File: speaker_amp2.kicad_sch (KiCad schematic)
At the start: 30 parts, among them U1 TAS5822MDCPR

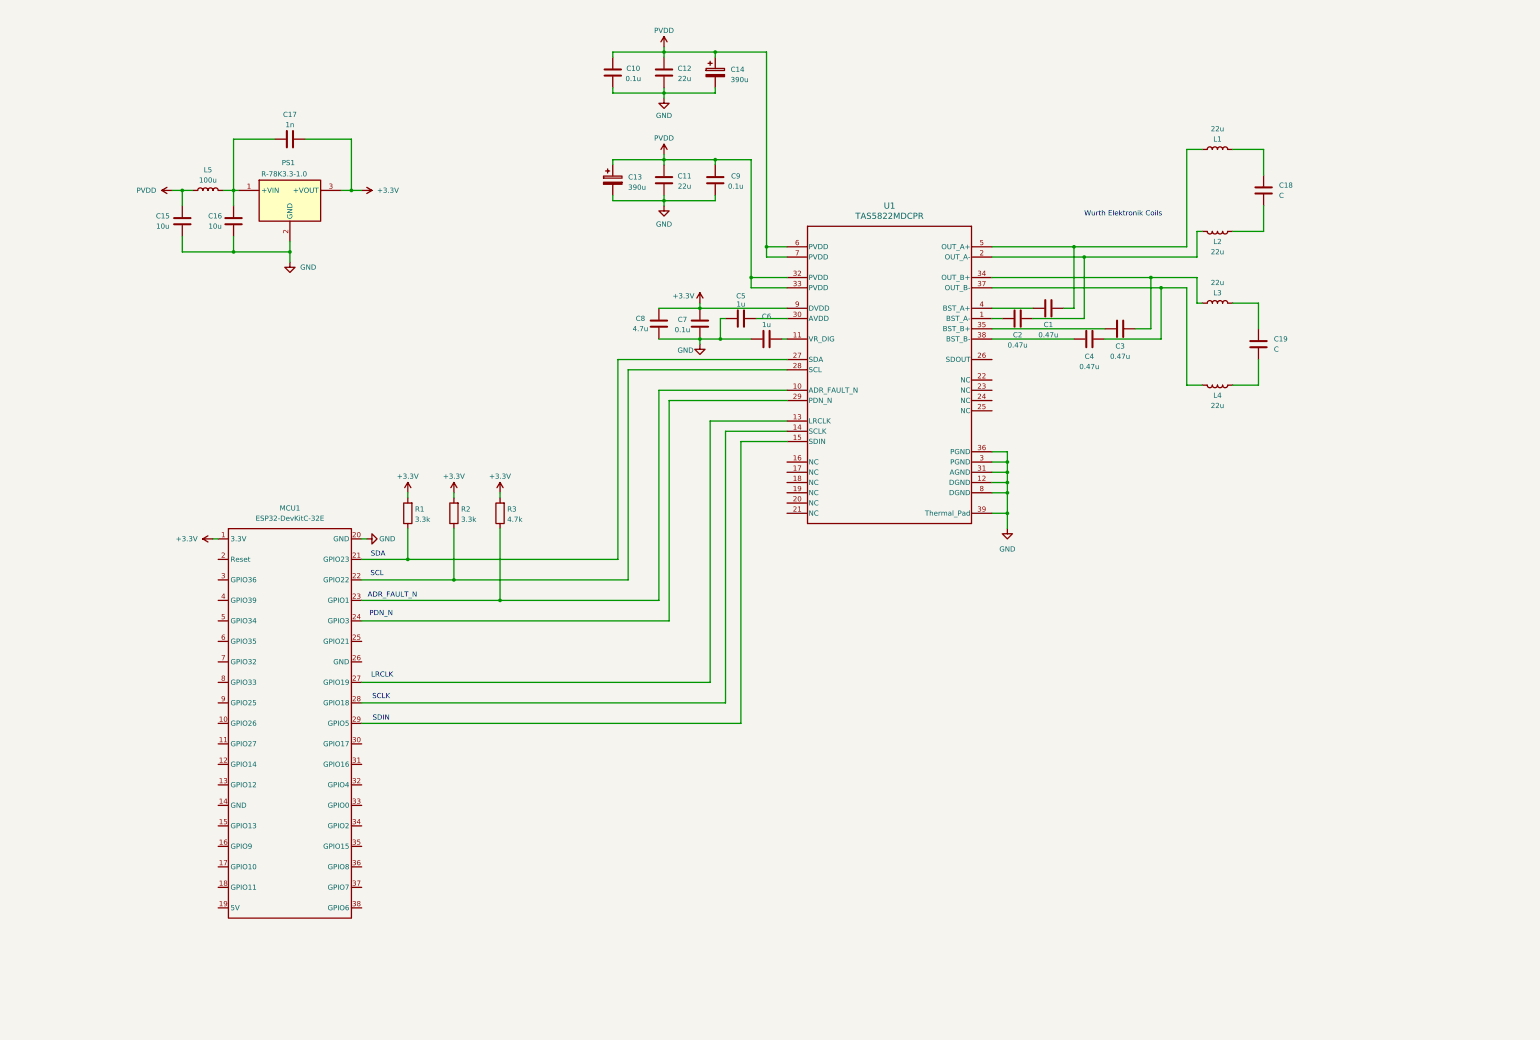
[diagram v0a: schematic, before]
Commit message: added C_g cap
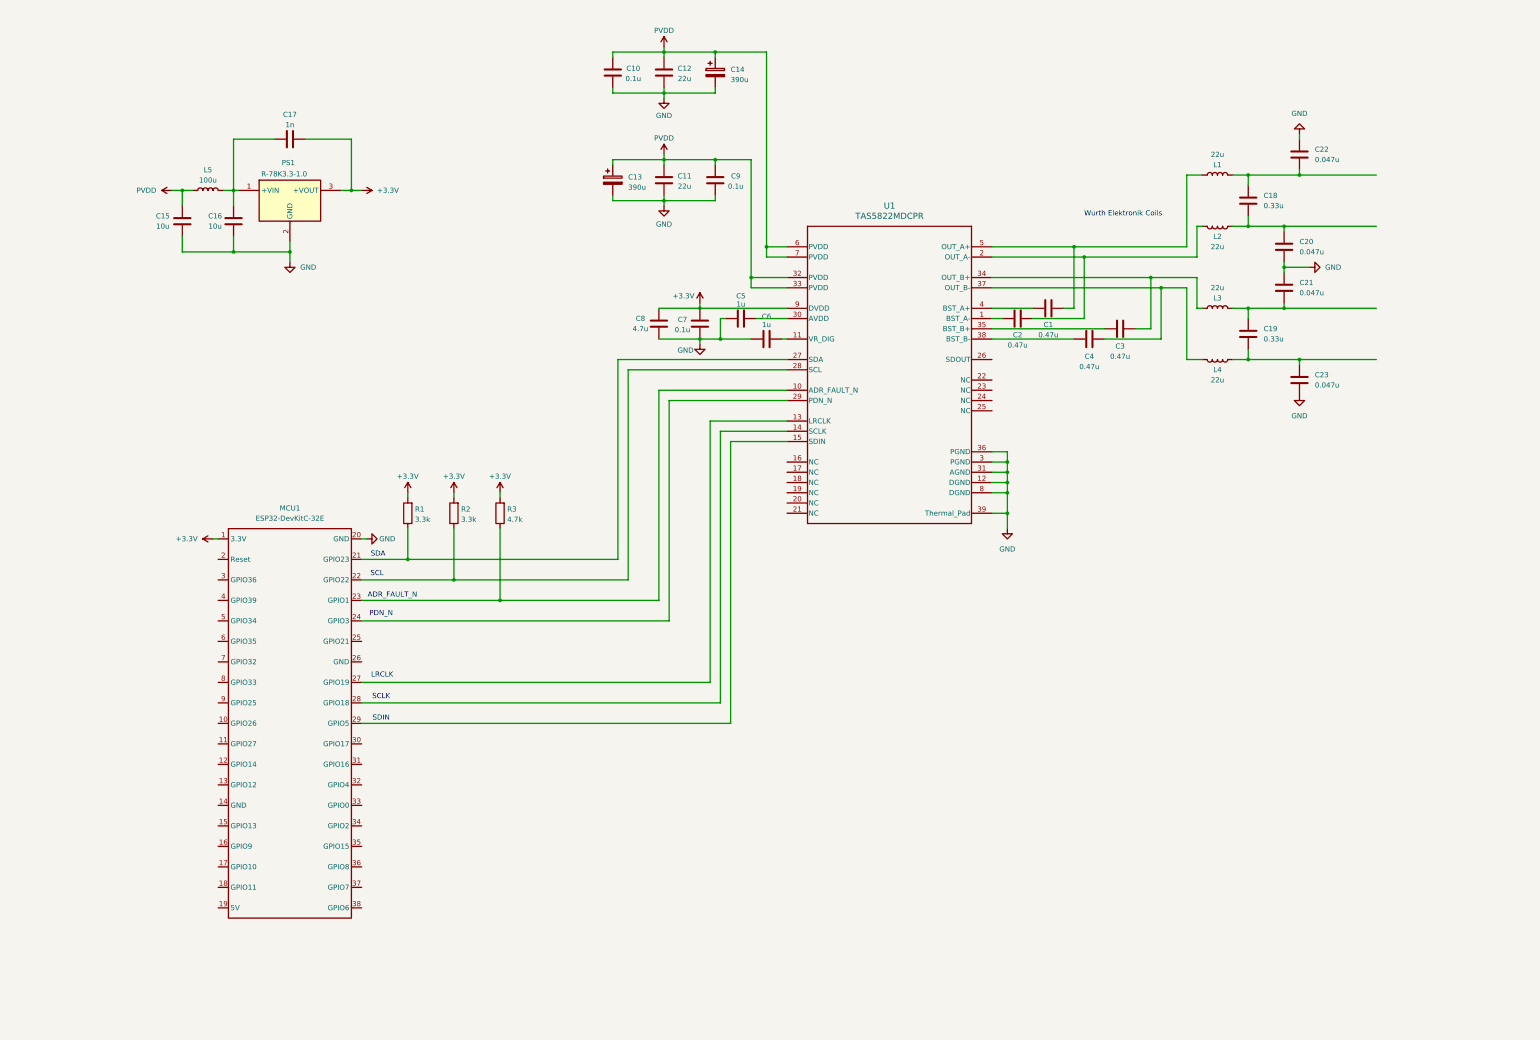
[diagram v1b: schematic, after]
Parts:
- added C20, C21, C22, C23: 0.047u, Capacitor_THT:C_Rect_L13.0mm_W5.0mm_P10.00mm_FKS3_FKP3_MKS4, symbol Device:C
- C18, C19: value C -> 0.33u
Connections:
- net GND: now also C20.2, C21.1, C22.1, C23.2
- net at C18.2, L2.1: now also C20.1
- net at C18.1, L1.2: now also C22.2
- net at C19.2, L4.1: now also C23.1
- net at C19.1, L3.2: now also C21.2
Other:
- moved on the sheet: C18, L1, L2, L3, L4

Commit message: added 2nd TAS5822M
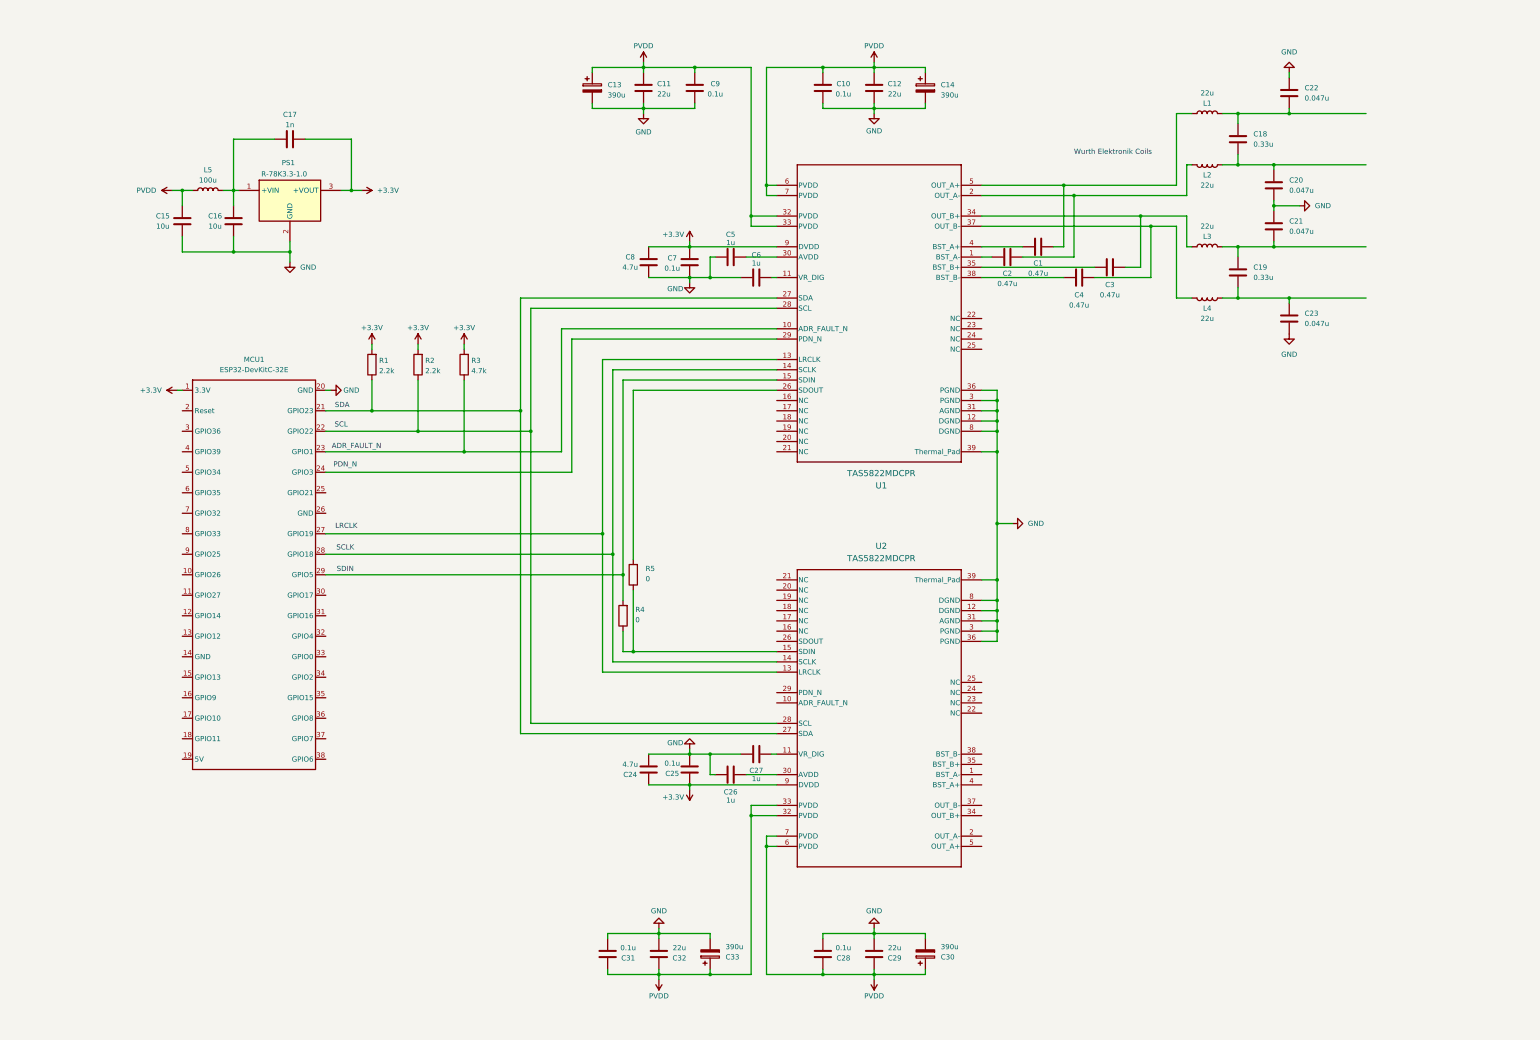
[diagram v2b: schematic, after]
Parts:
- added C24: 4.7u, Capacitor_SMD:C_0805_2012Metric_Pad1.18x1.45mm_HandSolder, symbol Device:C
- added C25, C28, C31: 0.1u, Capacitor_SMD:C_0805_2012Metric_Pad1.18x1.45mm_HandSolder, symbol Device:C
- added C26, C27: 1u, Capacitor_SMD:C_0805_2012Metric_Pad1.18x1.45mm_HandSolder, symbol Device:C
- added C29, C32: 22u, Capacitor_SMD:C_1210_3225Metric_Pad1.33x2.70mm_HandSolder, symbol Device:C
- added C30, C33: 390u, Capacitor_THT:CP_Radial_D8.0mm_P3.50mm, symbol Device:C_Polarized
- added R4, R5: 0, Resistor_SMD:R_0805_2012Metric_Pad1.20x1.40mm_HandSolder, symbol Device:R
- added U2: TAS5822MDCPR, DCP0038A-IPC_A, symbol Speaker Amp Lib:TAS5822MDCPR
- R1, R2: value 3.3k -> 2.2k; MouserLink https://gr.mouser.com/ProductDetail/YAGEO/RT0805DRD073K3L?q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 -> https://gr.mouser.com/ProductDetail/YAGEO/RT0805FRE132K2L?q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
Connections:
- net +3.3V: now also C24.2, C25.2, U2.9 (DVDD)
- net GND: now also C24.1, C25.1, C26.2, C27.2, C28.1, C29.1, C30.2, C31.1, C32.1, C33.2, U2.12 (DGND), U2.3 (PGND), U2.31 (AGND), U2.36 (PGND), U2.39 (Thermal_Pad), U2.8 (DGND)
- net PVDD: now also C28.2, C29.2, C30.1, C31.2, C32.2, C33.1, U2.32 (PVDD), U2.33 (PVDD), U2.6 (PVDD), U2.7 (PVDD)
- net at MCU1.22 (GPIO22), R2.1, U1.28 (SCL): now also U2.28 (SCL)
- net at MCU1.21 (GPIO23), R1.1, U1.27 (SDA): now also U2.27 (SDA)
- net at MCU1.27 (GPIO19), U1.13 (LRCLK): now also U2.13 (LRCLK)
- net at MCU1.28 (GPIO18), U1.14 (SCLK): now also U2.14 (SCLK)
- net at MCU1.29 (GPIO5), U1.15 (SDIN): now also R4.2
- net at U1.26 (SDOUT): now also R5.2
- new net: C26.1, U2.30 (AVDD)
- new net: C27.1, U2.11 (VR_DIG)
- new net: R4.1, R5.1, U2.15 (SDIN)
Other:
- moved on the sheet: C1, C10, C11, C12, C13, C14, C18, C19, C2, C20, C21, C22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

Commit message: added mono ch bootstrap caps
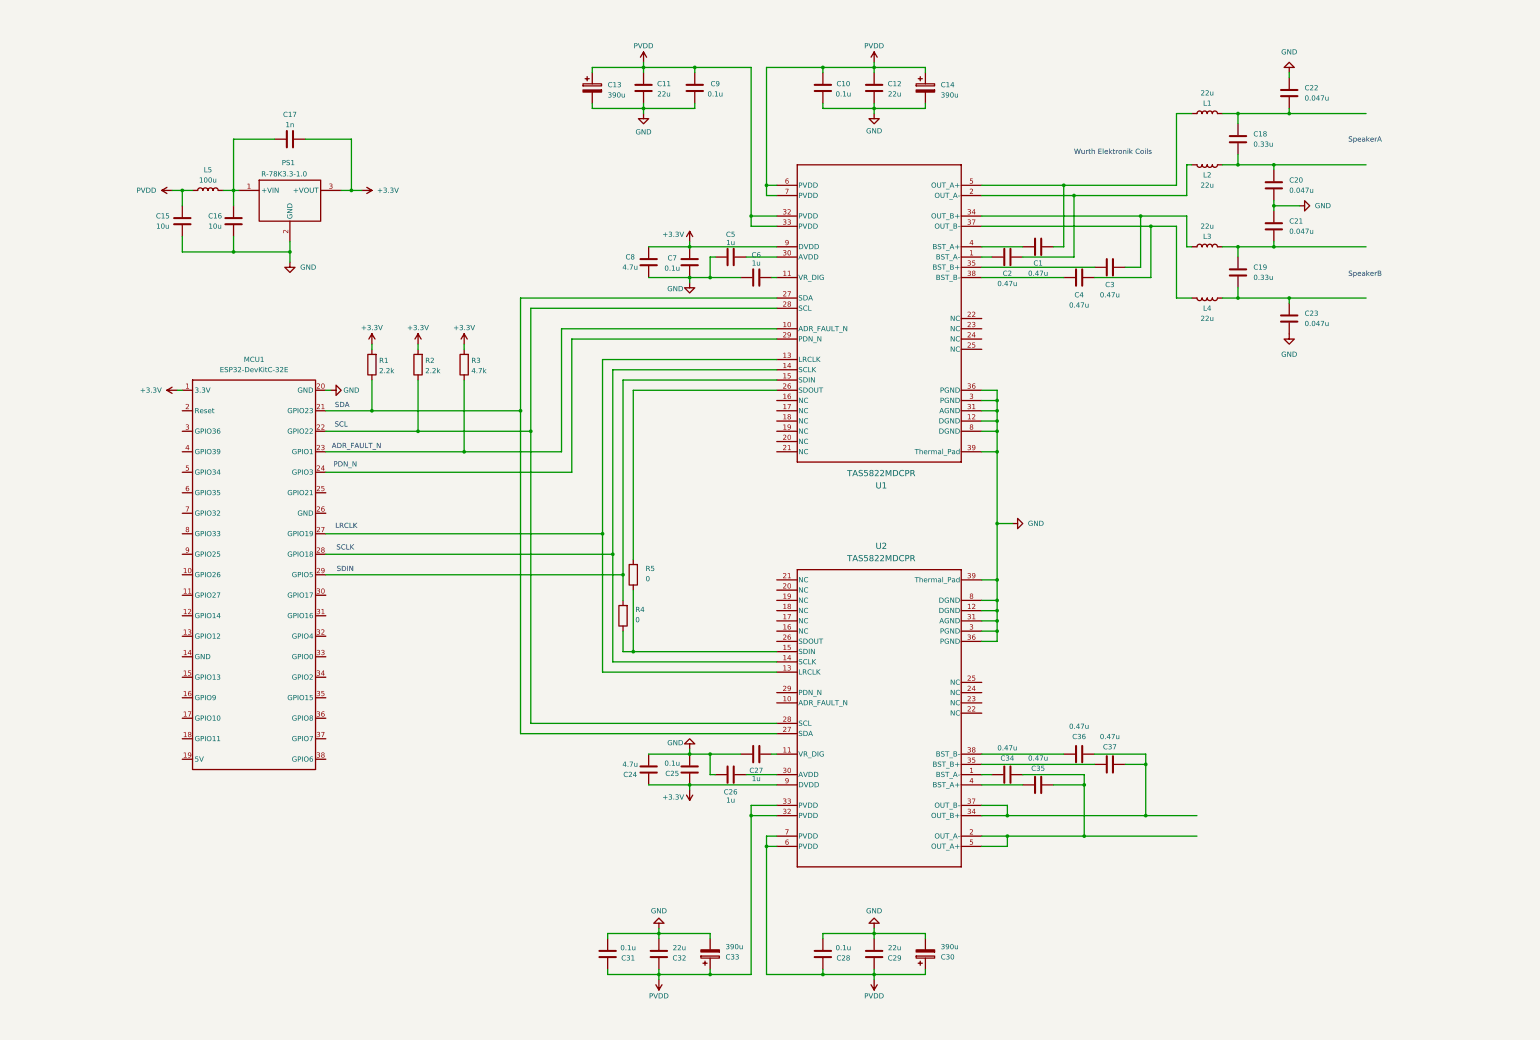
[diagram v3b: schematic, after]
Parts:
- added C34, C35, C36, C37: 0.47u, Capacitor_SMD:C_0805_2012Metric_Pad1.18x1.45mm_HandSolder, symbol Device:C
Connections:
- net at U2.1 (BST_A-): now also C34.1
- net at U2.2 (OUT_A-): now also U2.5 (OUT_A+), C34.2, C35.2
- net at U2.34 (OUT_B+): now also U2.37 (OUT_B-), C36.2, C37.2
- net at U2.35 (BST_B+): now also C37.1
- net at U2.38 (BST_B-): now also C36.1
- net at U2.4 (BST_A+): now also C35.1
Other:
- note added: "SpeakerA"
- note added: "SpeakerB"

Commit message: finished first iteration, connectors wip
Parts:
- added C38: 0.68u, Capacitor_THT:C_Rect_L18.0mm_W13.0mm_P15.00mm_FKS3_FKP3, symbol Device:C
- added C39, C40: 0.1u, Capacitor_THT:C_Rect_L18.0mm_W5.0mm_P15.00mm_FKS3_FKP3, symbol Device:C
- added L6, L7: 10u, Inductor_SMD:L_Wuerth_WE-PD-Typ-LS_Handsoldering, symbol Device:L
- added R6: 15k, Resistor_SMD:R_0805_2012Metric_Pad1.20x1.40mm_HandSolder, symbol Device:R
- added R7, R8: 4.7k, Resistor_SMD:R_0805_2012Metric_Pad1.20x1.40mm_HandSolder, symbol Device:R
- MCU1: MouserLink (none) -> https://gr.mouser.com/ProductDetail/Espressif-Systems/ESP32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
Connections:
- net +3.3V: now also R6.2
- net GND: now also C39.2, C40.2, R7.2, R8.2
- net at C34.2, C35.2, U2.2 (OUT_A-)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: now also L7.2
- net at C36.2, C37.2, U2.34 (OUT_B+)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: now also L6.1
- net at MCU1.24 (GPIO3), U1.29 (PDN_N): now also R7.1
- net at MCU1.30 (GPIO17): now also U2.29 (PDN_N), R8.1
- net at MCU1.31 (GPIO16): now also U2.10 (ADR_FAULT_N), R6.1
- new net: C38.1, C40.1, L6.2
- new net: C38.2, C39.1, L7.1
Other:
- note added: "ADR_FAULT_N_2"
- note added: "PDN_N_2"
- note added: "SpeakerA 8Ω"
- note added: "SpeakerB 8Ω"
- note added: "SpeakerC 4Ω"
- note removed: "SpeakerA"
- note removed: "SpeakerB"
- moved on the sheet: C1, C10, C11, C12, C13, C14, C15, C16, C17, C18, C19, C2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
